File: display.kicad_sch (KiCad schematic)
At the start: 38 parts, among them J2 Conn_02x19_Odd_Even, Q13 2N3904, Q14 2N3904, Q15 2N3904, Q16 2N3904, Q17 2N3904, Q18 2N3904, Q19 2N3904, Q20 2N3904, Q21 AO3401A, Q22 AO3401A, Q23 AO3401A, Q24 AO3401A, U2 CC56-12EWA

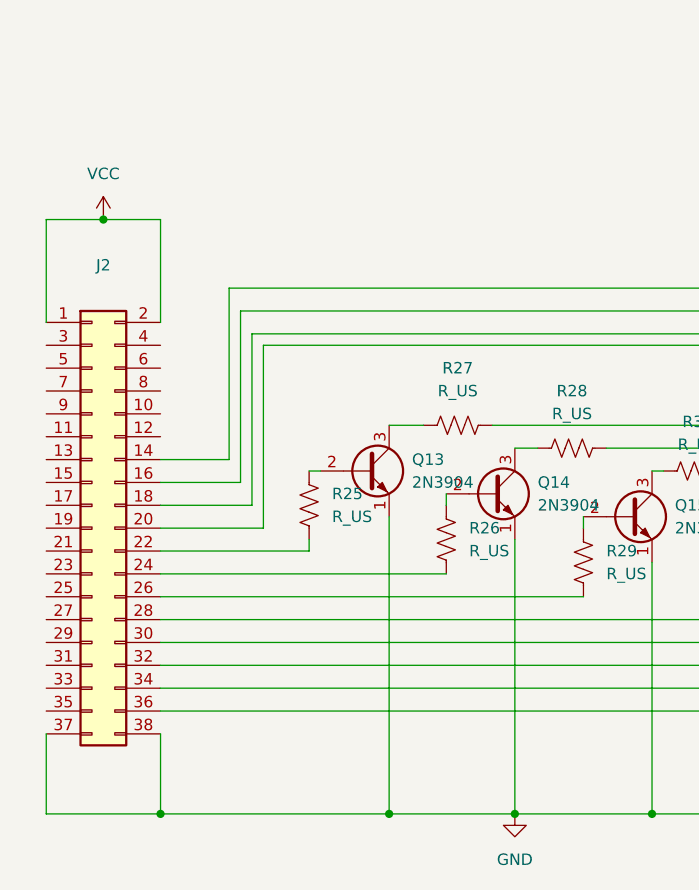
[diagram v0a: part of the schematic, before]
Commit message: Updated sheet connections for MCU to Display
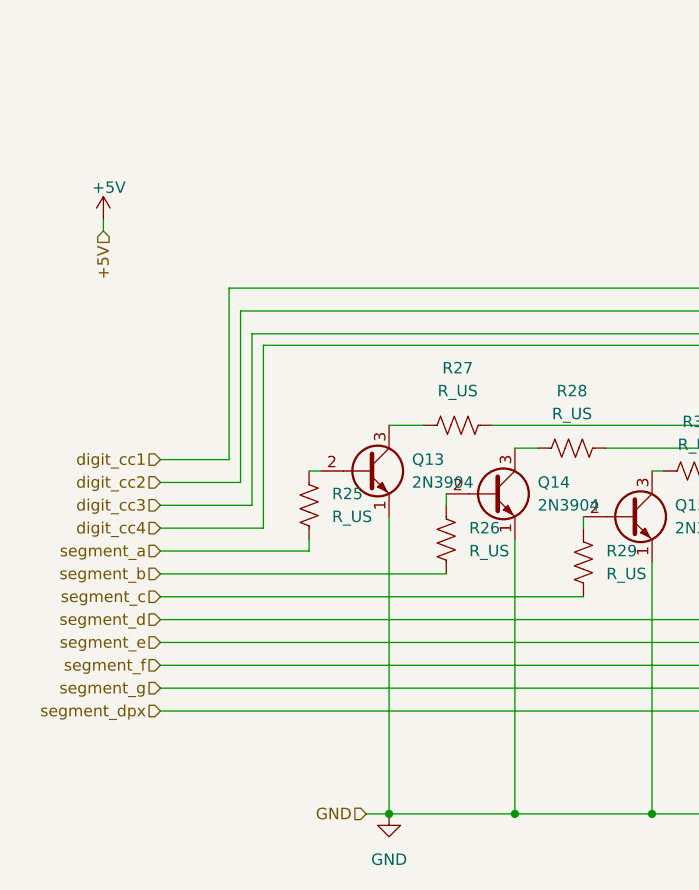
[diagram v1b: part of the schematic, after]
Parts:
- removed J2: Conn_02x19_Odd_Even, Connector_PinSocket_2.54mm:PinSocket_2x38_P2.54mm_Vertical, symbol Connector_Generic:Conn_02x19_Odd_Even
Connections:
- net segment_a: now reaches R25.1
- net segment_d: now reaches R31.2
- net segment_c: now reaches R29.2
- net digit_cc4: now reaches R48.2
- net digit_cc2: now reaches R44.2
- net segment_b: now reaches R26.1
- net segment_g: now reaches R37.2
- net segment_dpx: now reaches R39.2
- net digit_cc1: now reaches R42.2
- net digit_cc3: now reaches R46.2
- net segment_e: now reaches R33.2
- net segment_f: now reaches R35.2

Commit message: Updated the display type
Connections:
- net VCC is gone; now on net +5V: Q21.3 (D), Q22.3 (D), Q23.3 (D), Q24.3 (D), R41.1, R43.1, R45.1, R47.1
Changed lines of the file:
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@@
 		(in_pos_files yes)
 		(dnp no)
-		(fields_autoplaced yes)
 		(property "Reference" "#PWR06"
 			(at 226.06 60.96 0)
@@
 			)
 		)
-		(property "Value" "VCC"
-			(at 226.06 52.07 0)
+		(property "Value" "+5V"
+			(at 224.79 53.34 0)
 			(show_name no)
 			(do_not_autoplace no)
@@
 					(size 1.27 1.27)
 				)
+				(justify left)
 			)
 		)
